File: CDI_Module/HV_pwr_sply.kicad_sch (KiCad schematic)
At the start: 16 parts, among them Q1 Q_NMOS_GDS, Q2 BC237, U1 NE555P

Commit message: Work in progress
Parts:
- removed Q1: Q_NMOS_GDS, Package_TO_SOT_THT:TO-220-3_Vertical, symbol Device:Q_NMOS_GDS
- removed Q2: BC237, Package_TO_SOT_THT:TO-92_Inline, symbol Transistor_BJT:BC237
- removed R4: 10k, Resistor_THT:R_Axial_DIN0207_L6.3mm_D2.5mm_P10.16mm_Horizontal, symbol Device:R
- added Q1: IRF3205, Package_TO_SOT_THT:TO-220-3_Vertical, symbol Transistor_FET:IRF3205
- added R9: 1k, Resistor_THT:R_Axial_DIN0207_L6.3mm_D2.5mm_P10.16mm_Horizontal, symbol Device:R
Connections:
- net GND: now also Q1.3 (S)
- net PULSE: now also R3.1, R9.1
- net at D1.2 (A), L1.2: now also Q1.2 (D)
- new net: Q1.1 (G), R9.2

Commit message: Tiny modification
???
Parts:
- removed C3: 100n, Capacitor_THT:C_Rect_L7.0mm_W2.5mm_P5.00mm, symbol Device:C
- removed D2: 1n4007, symbol Device:D
- removed Q1: IRF3205, Package_TO_SOT_THT:TO-220-3_Vertical, symbol Transistor_FET:IRF3205
- added C3: 10uF / 100V, symbol Device:C_Polarized
- added Q2: NMOS, Package_TO_SOT_THT:TO-220-3_Vertical, symbol Simulation_SPICE:NMOS
- L1: value 100uH -> 470uH
- R1: value 200k -> 6k6
- R2: value 100k -> 3k3
- R3: value 10k -> 1k
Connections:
- net GND: now also C3.2, Q2.3 (S)
- net HT: now also D1.1 (K), C3.1
- net at R9.2: now also Q2.2 (G)
- net at D1.2 (A), L1.2: now also Q2.1 (D)
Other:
- note added: "Dimentionnement oscillateur : VOut = 10,5V f = 109,295 kHz Duty Cycle = 75% T = 9,15 us T(up) = 6,862 us T(down) = 2,287 us"
- note removed: "Dimentionnement oscillateur : VOut = 10,5V f = 3,607 kHz Duty Cycle = 75% T = 277 us"
- note removed: "Don't know if D2 is usefull"
- moved on the sheet: C1

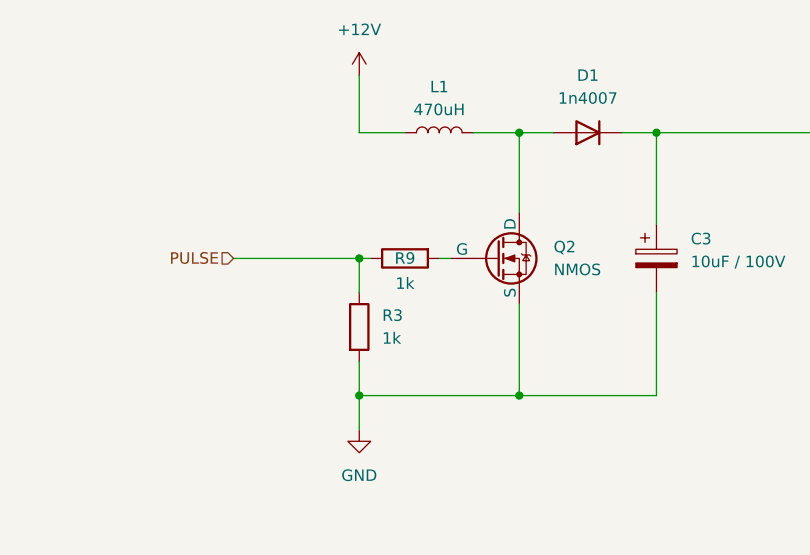
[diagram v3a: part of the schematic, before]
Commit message: Designed a minimal external coil driver
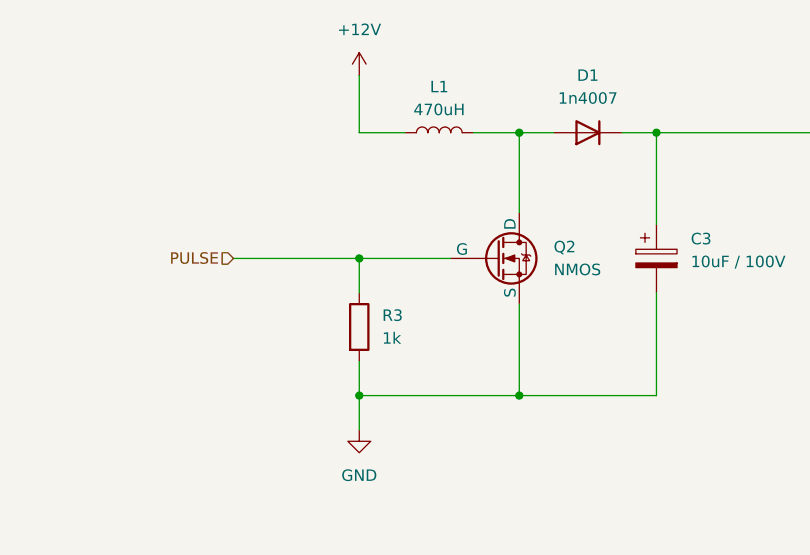
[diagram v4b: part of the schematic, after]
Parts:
- removed R9: 1k, Resistor_THT:R_Axial_DIN0207_L6.3mm_D2.5mm_P10.16mm_Horizontal, symbol Device:R
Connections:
- net PULSE: now also Q2.2 (G)
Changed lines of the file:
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@@
 	(wire
 		(pts
-			(xy 170.18 49.53) (xy 171.45 49.53)
+			(xy 170.18 49.53) (xy 180.34 49.53)
 		)
 		(stroke
@@
 		(pts
 			(xy 167.64 124.46) (xy 168.91 124.46)
-		)
-		(stroke
-			(width 0)
-			(type default)
-		)
-	)
-	(wire
-		(pts
-			(xy 179.07 49.53) (xy 180.34 49.53)
 		)
 		(stroke
@@
 					(unit 1)
 				)
-			)
-		)
-	)
-	(symbol
-		(lib_id "Device:R")
-		(at 175.26 49.53 90)
-		(mirror x)
-		(unit 1)
-		(exclude_from_sim yes)
-		(in_bom yes)
-		(on_board yes)
-		(dnp no)
-		(property "Reference" "R9"
-			(at 175.26 49.53 90)
-			(effects
-				(font
-					(size 1.27 1.27)
-				)
-			)
-		)
-		(property "Value" "1k"
-			(at 175.26 52.324 90)
-			(effects
-				(font
-					(size 1.27 1.27)
-				)
-			)
-		)
-		(property "Footprint" "Resistor_THT:R_Axial_DIN0207_L6.3mm_D2.5mm_P10.16mm_Horizontal"
-			(at 175.26 47.752 90)
-			(effects
-				(font
-					(size 1.27 1.27)
-				)
-				(hide yes)
-			)
-		)
-		(property "Datasheet" "~"
-			(at 175.26 49.53 0)
-			(effects
-				(font
-					(size 1.27 1.27)
-				)
-				(hide yes)
-			)
-		)
-		(property "Description" "Resistor"
-			(at 175.26 49.53 0)
-			(effects
-				(font
-					(size 1.27 1.27)
-				)
-				(hide yes)
-			)
-		)
-		(pin "1"
-		)
-		(pin "2"
-		)
-		(instances
-			(project "CDI_Module"
-				(path "/a4713233-3633-4d06-9186-8236551fb01a/0d28dddc-bb20-4ced-8840-72b43d7554f4"
-					(reference "R9")
-					(unit 1)
-				)
